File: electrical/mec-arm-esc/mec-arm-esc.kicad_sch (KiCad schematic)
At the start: 0 parts

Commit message: added backups
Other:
- sheet mcu: file untitled.kicad_sch -> mcu.kicad_sch
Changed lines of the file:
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@@
 	)
 	(sheet
-		(at 127 60.96)
-		(size 48.26 78.74)
+		(at 114.3 59.69)
+		(size 43.18 81.28)
 		(exclude_from_sim no)
 		(in_bom yes)
@@
 		)
 		(fill
-			(color 110 124 255 1)
+			(color 0 0 0 0)
 		)
 		(property "Sheetname" "mcu"
-			(at 127 60.2484 0)
+			(at 114.3 58.9784 0)
 			(show_name no)
 			(do_not_autoplace no)
@@
 			)
 		)
-		(property "Sheetfile" "untitled.kicad_sch"
-			(at 127 140.2846 0)
+		(property "Sheetfile" "mcu.kicad_sch"
+			(at 114.3 141.5546 0)
 			(show_name no)
 			(do_not_autoplace no)

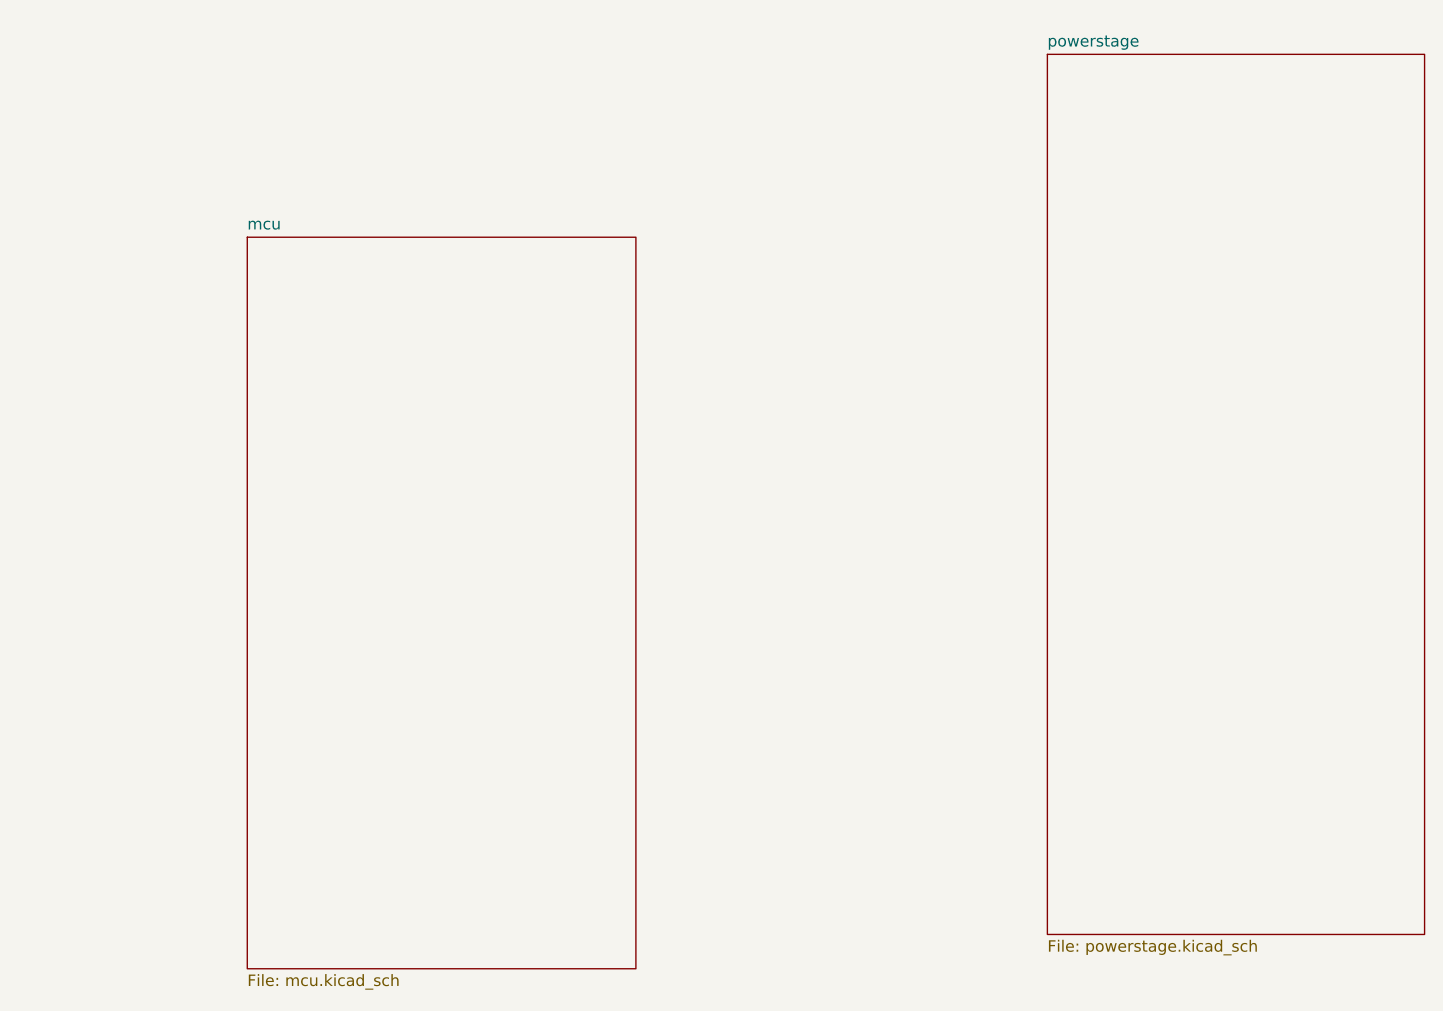
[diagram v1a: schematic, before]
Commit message: Finished Bare MCU + Oscillator, added prelim powerstage additions
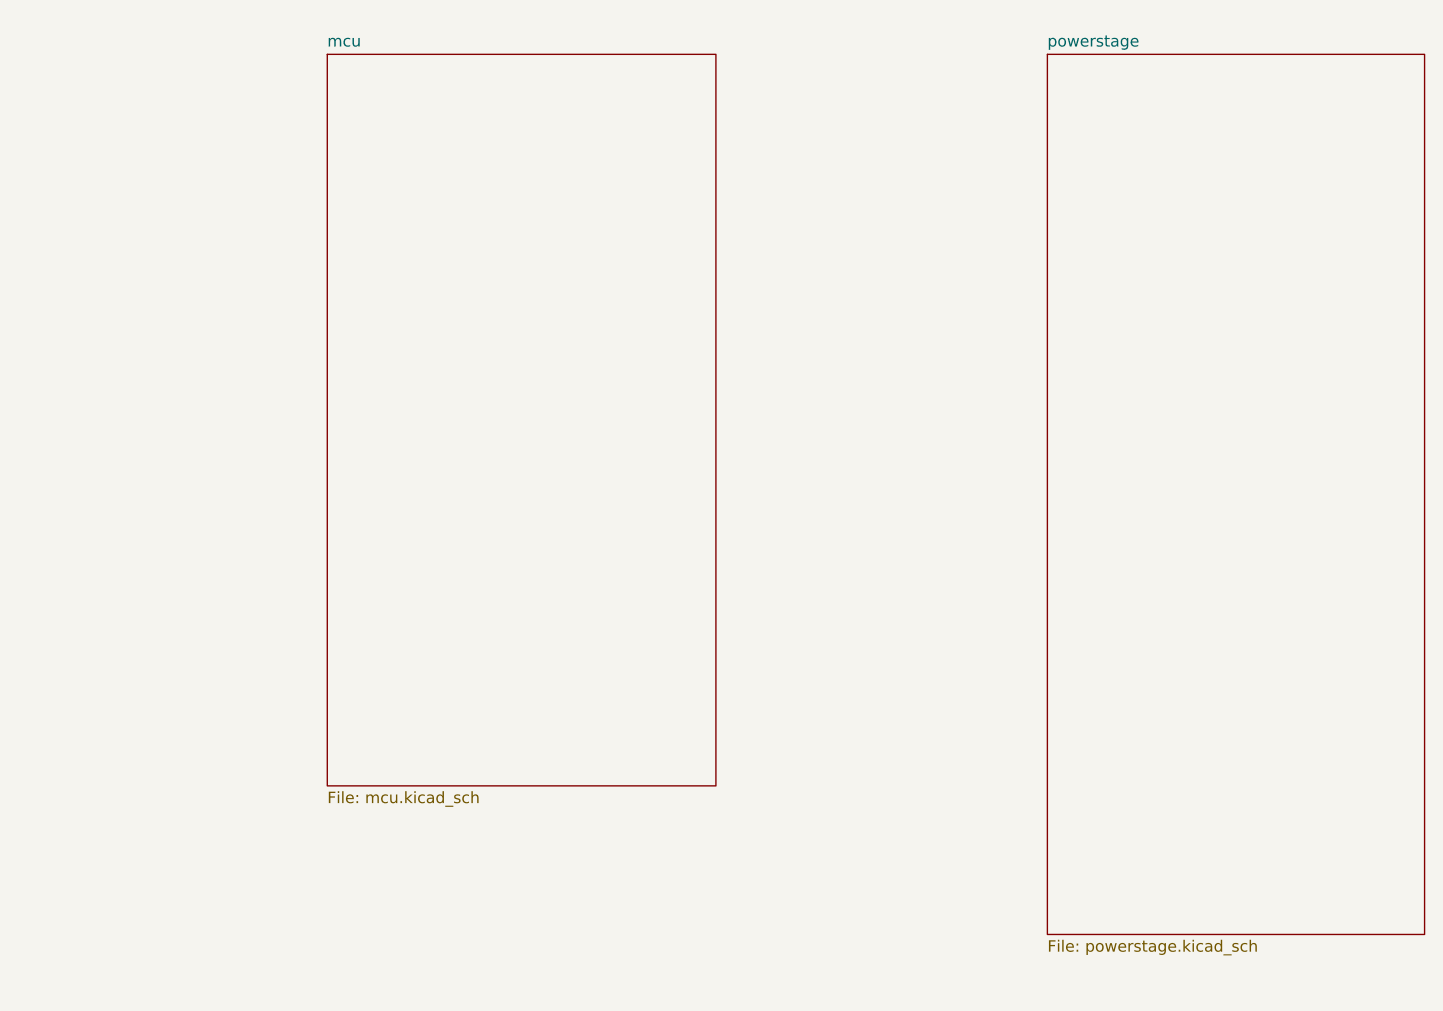
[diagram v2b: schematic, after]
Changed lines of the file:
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@@
 	)
 	(sheet
-		(at 114.3 59.69)
+		(at 123.19 39.37)
 		(size 43.18 81.28)
 		(exclude_from_sim no)
@@
 		)
 		(property "Sheetname" "mcu"
-			(at 114.3 58.9784 0)
+			(at 123.19 38.6584 0)
 			(show_name no)
 			(do_not_autoplace no)
@@
 		)
 		(property "Sheetfile" "mcu.kicad_sch"
-			(at 114.3 141.5546 0)
+			(at 123.19 121.2346 0)
 			(show_name no)
 			(do_not_autoplace no)

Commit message: Completed inverter, started calculation for input power
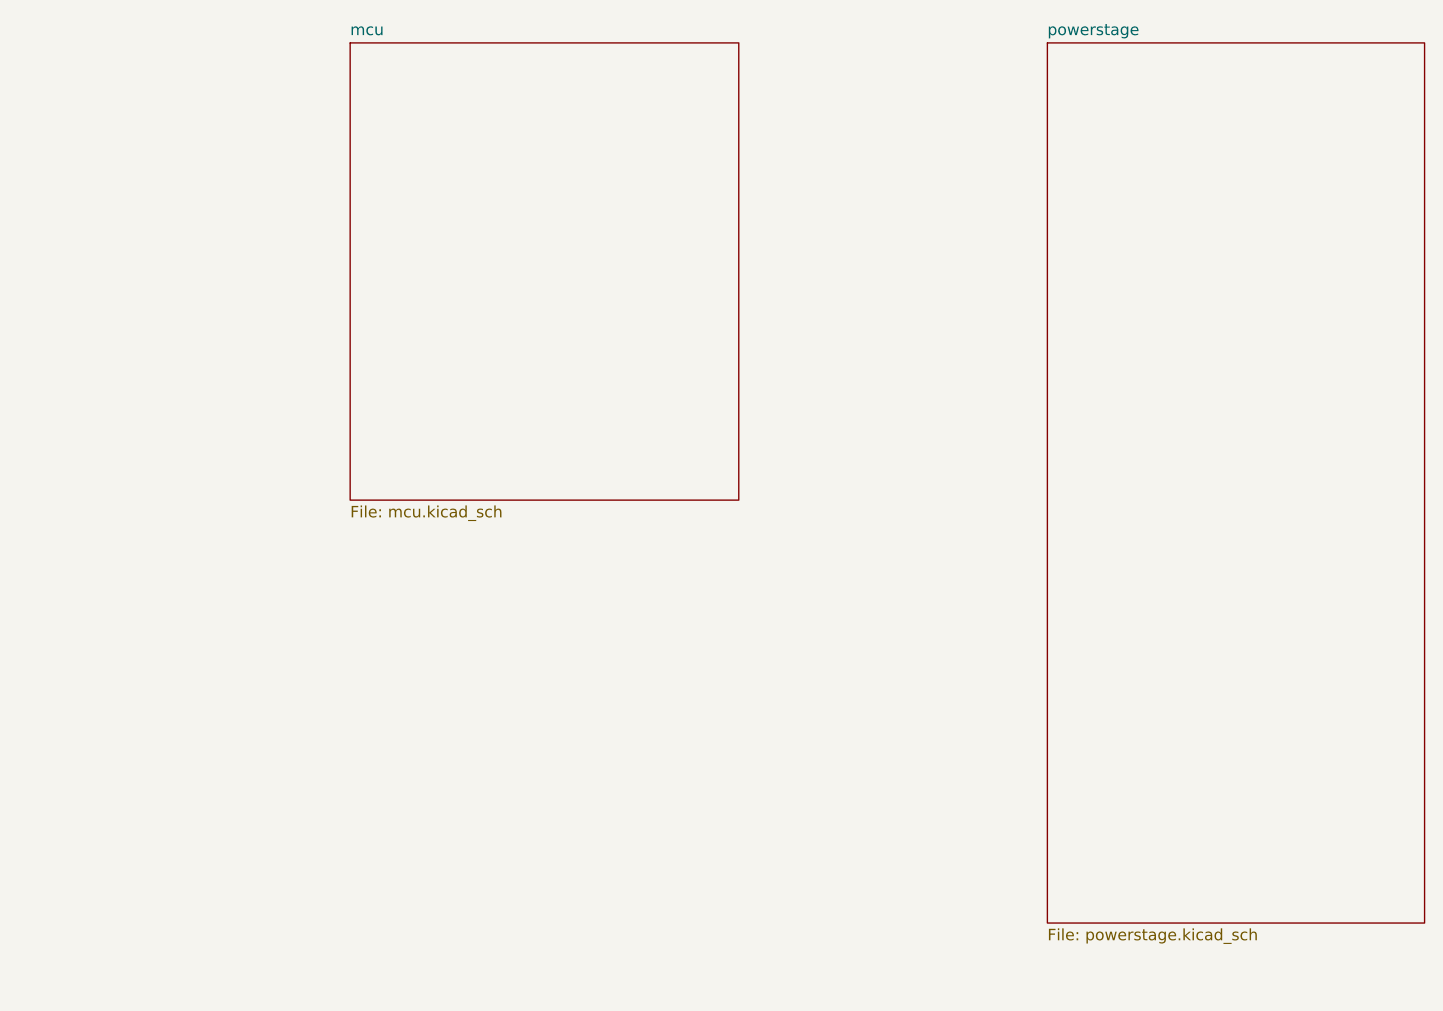
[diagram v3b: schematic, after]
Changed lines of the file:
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@@
 	)
 	(sheet
-		(at 203.2 39.37)
+		(at 203.2 38.1)
 		(size 41.91 97.79)
 		(exclude_from_sim no)
@@
 		)
 		(property "Sheetname" "powerstage"
-			(at 203.2 38.6584 0)
+			(at 203.2 37.3884 0)
 			(show_name no)
 			(do_not_autoplace no)
@@
 		)
 		(property "Sheetfile" "powerstage.kicad_sch"
-			(at 203.2 137.7446 0)
+			(at 203.2 136.4746 0)
 			(show_name no)
 			(do_not_autoplace no)
@@
 	)
 	(sheet
-		(at 123.19 39.37)
-		(size 43.18 81.28)
+		(at 125.73 38.1)
+		(size 43.18 50.8)
 		(exclude_from_sim no)
 		(in_bom yes)
@@
 		)
 		(property "Sheetname" "mcu"
-			(at 123.19 38.6584 0)
+			(at 125.73 37.3884 0)
 			(show_name no)
 			(do_not_autoplace no)
@@
 		)
 		(property "Sheetfile" "mcu.kicad_sch"
-			(at 123.19 121.2346 0)
+			(at 125.73 89.4846 0)
 			(show_name no)
 			(do_not_autoplace no)

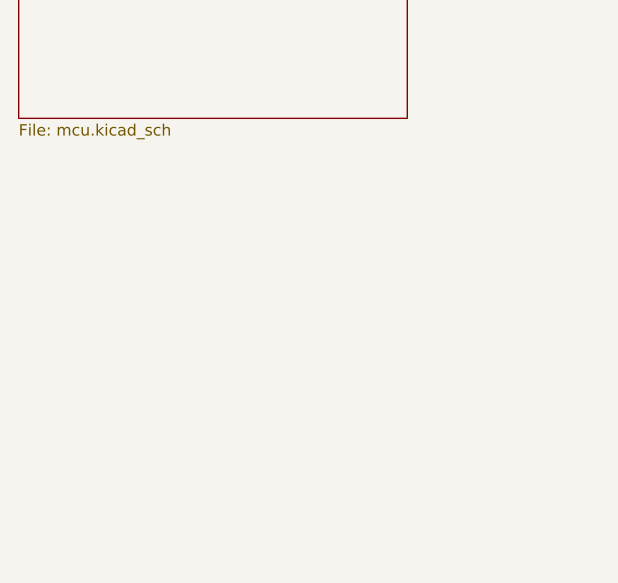
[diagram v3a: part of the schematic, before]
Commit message: Changed the components in all the drawings to reflect the new library, and added vbus sensing
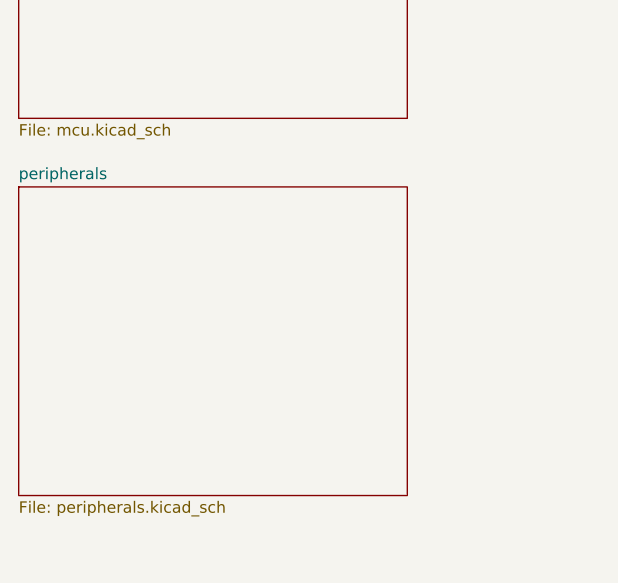
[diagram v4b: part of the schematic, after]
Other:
- added sheet peripherals (peripherals.kicad_sch)
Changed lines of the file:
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@@
+	)
+	(sheet
+		(at 125.73 96.52)
+		(size 43.18 34.29)
+		(exclude_from_sim no)
+		(in_bom yes)
+		(on_board yes)
+		(dnp no)
+		(fields_autoplaced yes)
+		(stroke
+			(width 0.1524)
+			(type solid)
+			(color 52 128 47 1)
+		)
+		(fill
+			(color 205 255 182 1)
+		)
+		(property "Sheetname" "peripherals"
+			(at 125.73 95.8084 0)
+			(show_name no)
+			(do_not_autoplace no)
+			(effects
+				(font
+					(size 1.27 1.27)
+				)
+				(justify left bottom)
+			)
+		)
+		(property "Sheetfile" "peripherals.kicad_sch"
+			(at 125.73 131.3946 0)
+			(show_name no)
+			(do_not_autoplace no)
+			(effects
+				(font
+					(size 1.27 1.27)
+				)
+				(justify left top)
+			)
+		)
+		(instances
+			(project "mec-arm-esc"
+				(path "/e8c42cac-0e93-4c5c-9b53-7b1f62cb177c"
+					(page "4")
+				)
+			)
+		)
 	)
 	(sheet
@@
 			(width 0.1524)
 			(type solid)
+			(color 88 98 173 1)
 		)
 		(fill
-			(color 0 0 0 0)
+			(color 151 177 255 1)
 		)
 		(property "Sheetname" "mcu"

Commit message: Schematic Done, review 1
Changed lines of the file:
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@@
 	)
 	(sheet
-		(at 203.2 38.1)
+		(at 166.37 40.64)
 		(size 41.91 97.79)
 		(exclude_from_sim no)
@@
 		)
 		(property "Sheetname" "powerstage"
-			(at 203.2 37.3884 0)
+			(at 166.37 39.9284 0)
 			(show_name no)
 			(do_not_autoplace no)
@@
 		)
 		(property "Sheetfile" "powerstage.kicad_sch"
-			(at 203.2 136.4746 0)
+			(at 166.37 139.0146 0)
 			(show_name no)
 			(do_not_autoplace no)
@@
 	)
 	(sheet
-		(at 125.73 96.52)
+		(at 88.9 99.06)
 		(size 43.18 34.29)
 		(exclude_from_sim no)
@@
 		)
 		(property "Sheetname" "peripherals"
-			(at 125.73 95.8084 0)
+			(at 88.9 98.3484 0)
 			(show_name no)
 			(do_not_autoplace no)
@@
 		)
 		(property "Sheetfile" "peripherals.kicad_sch"
-			(at 125.73 131.3946 0)
+			(at 88.9 133.9346 0)
 			(show_name no)
 			(do_not_autoplace no)
@@
 	)
 	(sheet
-		(at 125.73 38.1)
+		(at 88.9 40.64)
 		(size 43.18 50.8)
 		(exclude_from_sim no)
@@
 		)
 		(property "Sheetname" "mcu"
-			(at 125.73 37.3884 0)
+			(at 88.9 39.9284 0)
 			(show_name no)
 			(do_not_autoplace no)
@@
 		)
 		(property "Sheetfile" "mcu.kicad_sch"
-			(at 125.73 89.4846 0)
+			(at 88.9 92.0246 0)
 			(show_name no)
 			(do_not_autoplace no)

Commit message: Done placement, starting routing
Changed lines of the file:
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@@
 	(sheet
 		(at 88.9 99.06)
-		(size 43.18 34.29)
+		(size 43.18 39.37)
 		(exclude_from_sim no)
 		(in_bom yes)
@@
 		)
 		(property "Sheetfile" "peripherals.kicad_sch"
-			(at 88.9 133.9346 0)
+			(at 88.9 139.0146 0)
 			(show_name no)
 			(do_not_autoplace no)
